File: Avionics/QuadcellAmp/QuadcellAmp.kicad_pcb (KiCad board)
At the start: 2 copper layers, 10 parts, among them U2 OPA1679

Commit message: quadcell 1014
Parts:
- removed U1: ~, Library:Quadcell
- added CR1: PDB-C142, PDB-C142:PDB-C142_ADP, F.Cu at (117.0, 74.0)
- added CR2: PDB-C142, PDB-C142:PDB-C142_ADP, F.Cu at (111.5, 80.3)
- added CR3: PDB-C142, PDB-C142:PDB-C142_ADP, F.Cu at (122.5, 80.0)
- added CR4: PDB-C142, PDB-C142:PDB-C142_ADP, F.Cu at (117.0, 86.0)
- added D1: 1N4001, Diode_THT:D_DO-41_SOD81_P10.16mm_Horizontal, F.Cu at (146.5, 59.5)
- added D2: 1N4001, Diode_THT:D_DO-41_SOD81_P10.16mm_Horizontal, F.Cu at (153.0, 71.0)
- added D3: 1N4001, Diode_THT:D_DO-41_SOD81_P10.16mm_Horizontal, F.Cu at (146.4, 63.5)
- added D4: 1N4001, Diode_THT:D_DO-41_SOD81_P10.16mm_Horizontal, F.Cu at (153.0, 82.0)
- added D5: 1N4001, Diode_THT:D_DO-41_SOD81_P10.16mm_Horizontal, F.Cu at (153.0, 75.0)
- added D6: 1N4001, Diode_THT:D_DO-41_SOD81_P10.16mm_Horizontal, F.Cu at (153.0, 86.0)
- added D7: 1N4001, Diode_THT:D_DO-41_SOD81_P10.16mm_Horizontal, F.Cu at (153.0, 92.2)
- added D8: 1N4001, Diode_THT:D_DO-41_SOD81_P10.16mm_Horizontal, F.Cu at (153.0, 96.5)
- added J1: Screw_Terminal_01x02, TerminalBlock:TerminalBlock_Xinya_XY308-2.54-2P_1x02_P2.54mm_Horizontal, F.Cu at (104.5, 67.0)
- added R10: 40 Ω, Resistor_THT:R_Axial_DIN0204_L3.6mm_D1.6mm_P1.90mm_Vertical, F.Cu at (169.8, 87.1)
- added R11: 1 kΩ, Resistor_THT:R_Axial_DIN0204_L3.6mm_D1.6mm_P1.90mm_Vertical, F.Cu at (147.6, 69.5)
- added R12: 40 Ω, Resistor_THT:R_Axial_DIN0204_L3.6mm_D1.6mm_P1.90mm_Vertical, F.Cu at (169.8, 93.4)
- added R13: 4.6k, Resistor_THT:R_Axial_DIN0204_L3.6mm_D1.6mm_P1.90mm_Vertical, F.Cu at (103.6, 77.3)
- added R14: 4.7k, Resistor_THT:R_Axial_DIN0204_L3.6mm_D1.6mm_P1.90mm_Vertical, F.Cu at (103.6, 80.5)
- added R5: 1 kΩ, Resistor_THT:R_Axial_DIN0204_L3.6mm_D1.6mm_P1.90mm_Vertical, F.Cu at (140.1, 64.5)
- added R6: 1 kΩ, Resistor_THT:R_Axial_DIN0204_L3.6mm_D1.6mm_P1.90mm_Vertical, F.Cu at (139.1, 98.5)
- added R7: 40 Ω, Resistor_THT:R_Axial_DIN0204_L3.6mm_D1.6mm_P1.90mm_Vertical, F.Cu at (162.6, 61.5)
- added R8: 1 kΩ, Resistor_THT:R_Axial_DIN0204_L3.6mm_D1.6mm_P1.90mm_Vertical, F.Cu at (145.1, 97.0)
- added R9: 40 Ω, Resistor_THT:R_Axial_DIN0204_L3.6mm_D1.6mm_P1.90mm_Vertical, F.Cu at (167.1, 73.0)
- R1, R2, R3, R4: value R -> 100 kΩ
- U2: value OPA1679 -> LM324N; footprint Package_DIP:DIP-14_W7.62mm -> LM324:N14
- moved C2 27.4 mm to (108.2, 97.5)
- moved R2 25.1 mm to (108.6, 89.0)
- moved U2 18.1 mm to (146.6, 88.7)
- moved C3 10.0 mm to (128.0, 99.5)
- moved C4 8.98 mm to (118.2, 99.0)
- moved R4 8.64 mm to (118.6, 94.0)
- moved R3 7.65 mm to (128.6, 91.5)
- moved C1 1.12 mm to (126.5, 67.0)
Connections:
- U2 pad 11: /V_NEG -> GND
- U2 pad 13: GND -> QUAD_GND
- U2 pad 2: GND -> QUAD_GND
- U2 pad 4: /V_POS -> +BATT
- U2 pad 6: GND -> QUAD_GND
- U2 pad 9: GND -> QUAD_GND
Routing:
- net GND: track 98.3 -> 0.00 mm
- net /Anode_D: track 88.0 -> 0.14 mm
- net /Anode_C: track 68.5 -> 0.14 mm
- net Net-(C4-Pad2): track 62.1 -> 0.00 mm
- net /Anode_A: track 58.8 -> 0.22 mm
- net /Anode_B: track 53.7 -> 0.00 mm
- net Net-(C3-Pad2): track 38.5 -> 0.00 mm
- net Net-(C2-Pad2): track 35.0 -> 0.00 mm
- net Net-(C1-Pad2): track 33.5 -> 0.00 mm
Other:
- board text added: "Quadcell Amp v2.0"
- board text removed: "Quadcell Amp v1.0"

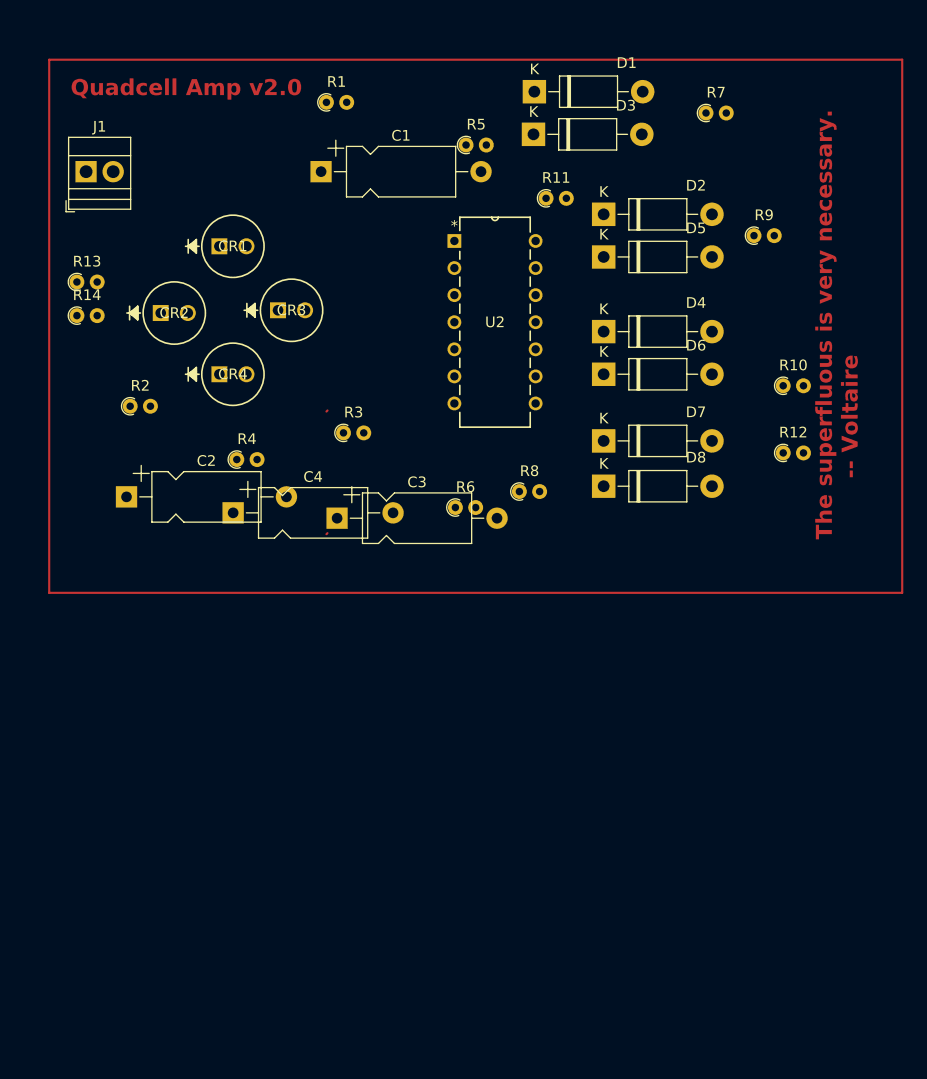
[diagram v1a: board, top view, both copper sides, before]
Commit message: Quadcell PD 2.0 finished
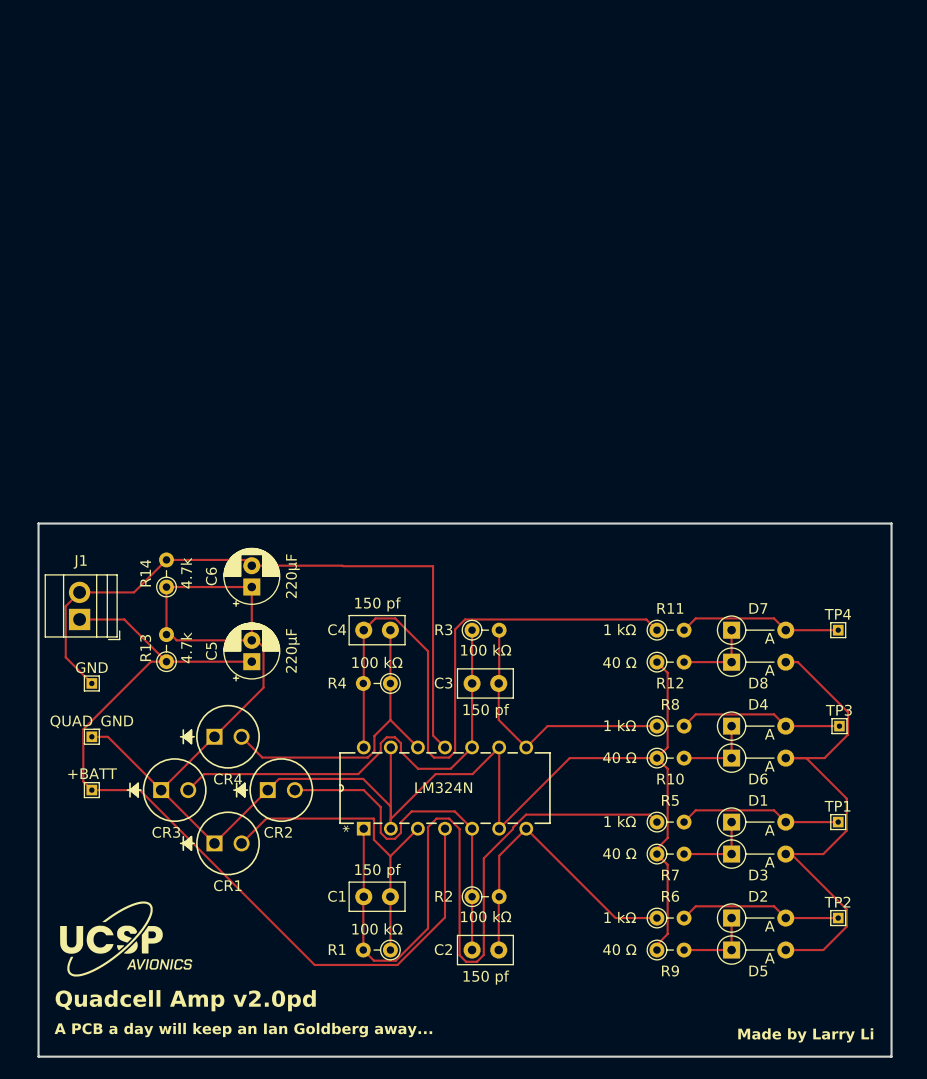
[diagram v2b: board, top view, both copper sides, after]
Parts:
- added +BATT: TestPoint, TestPoint:TestPoint_THTPad_1.0x1.0mm_Drill0.5mm, F.Cu at (105.0, 125.0)
- added C5: 220µF, Capacitor_THT:CP_Radial_D5.0mm_P2.00mm, F.Cu at (120.0, 113.0)
- added C6: 220µF, Capacitor_THT:CP_Radial_D5.0mm_P2.00mm, F.Cu at (120.0, 106.0)
- added G***: LOGO, UCSP:UCSP_avionics_logo, F.Cu at (107.0, 139.0)
- added GND: TestPoint, TestPoint:TestPoint_THTPad_1.0x1.0mm_Drill0.5mm, F.Cu at (105.0, 115.0)
- added QUAD_GND: TestPoint, TestPoint:TestPoint_THTPad_1.0x1.0mm_Drill0.5mm, F.Cu at (105.0, 120.0)
- added TP1: TestPoint, TestPoint:TestPoint_THTPad_1.0x1.0mm_Drill0.5mm, F.Cu at (175.0, 128.0)
- added TP2: TestPoint, TestPoint:TestPoint_THTPad_1.0x1.0mm_Drill0.5mm, F.Cu at (175.0, 137.0)
- added TP3: TestPoint, TestPoint:TestPoint_THTPad_1.0x1.0mm_Drill0.5mm, F.Cu at (175.1, 119.0)
- added TP4: TestPoint, TestPoint:TestPoint_THTPad_1.0x1.0mm_Drill0.5mm, F.Cu at (175.0, 110.0)
- C1, C2, C3, C4: value C -> 150 pf; footprint Capacitor_THT:CP_Axial_L10.0mm_D4.5mm_P15.00mm_Horizontal -> Capacitor_THT:C_Disc_D5.0mm_W2.5mm_P2.50mm
- D1, D2, D3, D4, D5, D6, D7, D8: value 1N4001 -> ~; footprint Diode_THT:D_DO-41_SOD81_P10.16mm_Horizontal -> Diode_THT:D_DO-35_SOD27_P5.08mm_Vertical_AnodeUp
- R1, R10, R11, R12, R14, R2, R3, R4, R5, R6, R7, R8, R9: footprint Resistor_THT:R_Axial_DIN0204_L3.6mm_D1.6mm_P1.90mm_Vertical -> Resistor_THT:R_Axial_DIN0204_L3.6mm_D1.6mm_P2.54mm_Vertical
- R13: value 4.6k -> 4.7k; footprint Resistor_THT:R_Axial_DIN0204_L3.6mm_D1.6mm_P1.90mm_Vertical -> Resistor_THT:R_Axial_DIN0204_L3.6mm_D1.6mm_P2.54mm_Vertical
- moved R1 79.7 mm to (133.0, 140.0), turned to 180 degrees
- moved D1 71.0 mm to (165.0, 128.0)
- moved D3 70.0 mm to (165.0, 131.0)
- moved R7 69.7 mm to (158.0, 131.0)
- moved C1 68.3 mm to (133.0, 135.0), turned to 180 degrees
- moved R9 67.6 mm to (158.0, 140.0)
- moved D2 67.1 mm to (165.0, 137.0)
- moved D5 66.1 mm to (165.0, 140.0)
- moved R5 66.0 mm to (158.0, 128.0)
- moved R2 56.1 mm to (140.7, 135.0)
- moved CR1 56.0 mm to (116.5, 130.0)
- moved C2 53.4 mm to (140.7, 140.0)
- moved CR3 46.3 mm to (111.5, 125.0)
- moved CR2 45.9 mm to (121.5, 125.0)
- moved R6 42.9 mm to (158.0, 137.0)
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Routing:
- net QUAD_GND: track 0.00 -> 158.4 mm
- net +BATT: track 0.00 -> 84.2 mm
- net Net-(C1-Pad2): track 0.00 -> 74.3 mm
- net Net-(C4-Pad2): track 0.00 -> 62.4 mm
- net GND: track 0.00 -> 61.7 mm
- net 3V3: track 0.00 -> 49.7 mm
- net /Anode_C: track 0.14 -> 42.6 mm
- net /Anode_B: track 0.00 -> 33.6 mm
- net /Anode_A: track 0.22 -> 30.0 mm
- net /Anode_D: track 0.14 -> 29.1 mm
- net Net-(C2-Pad2): track 0.00 -> 28.2 mm
- net Net-(C3-Pad2): track 0.00 -> 25.2 mm
- net Net-(D4-A): track 0.00 -> 15.5 mm
- net Net-(D7-A): track 0.00 -> 15.4 mm
- net Net-(D2-A): track 0.00 -> 15.4 mm
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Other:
- board outline added: 80 x 50 mm
- board text added: "A PCB a day will keep an Ian Goldberg away..."
- board text added: "Made by Larry Li"
- board text added: "Quadcell Amp v2.0pd"
- board text removed: "Quadcell Amp v2.0"
- board text removed: "The superfluous is very necessary. -- Voltaire"

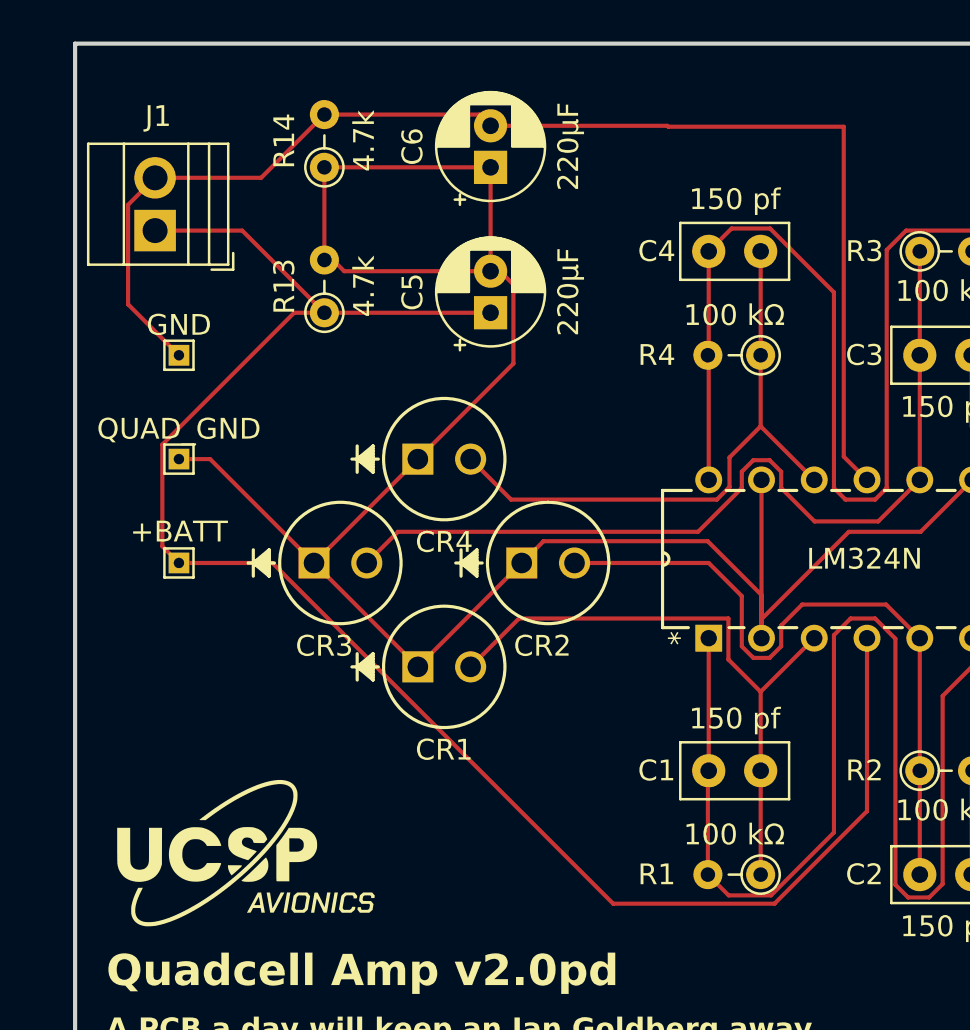
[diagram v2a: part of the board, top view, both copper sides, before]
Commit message: added USA flags to pulse footprint library
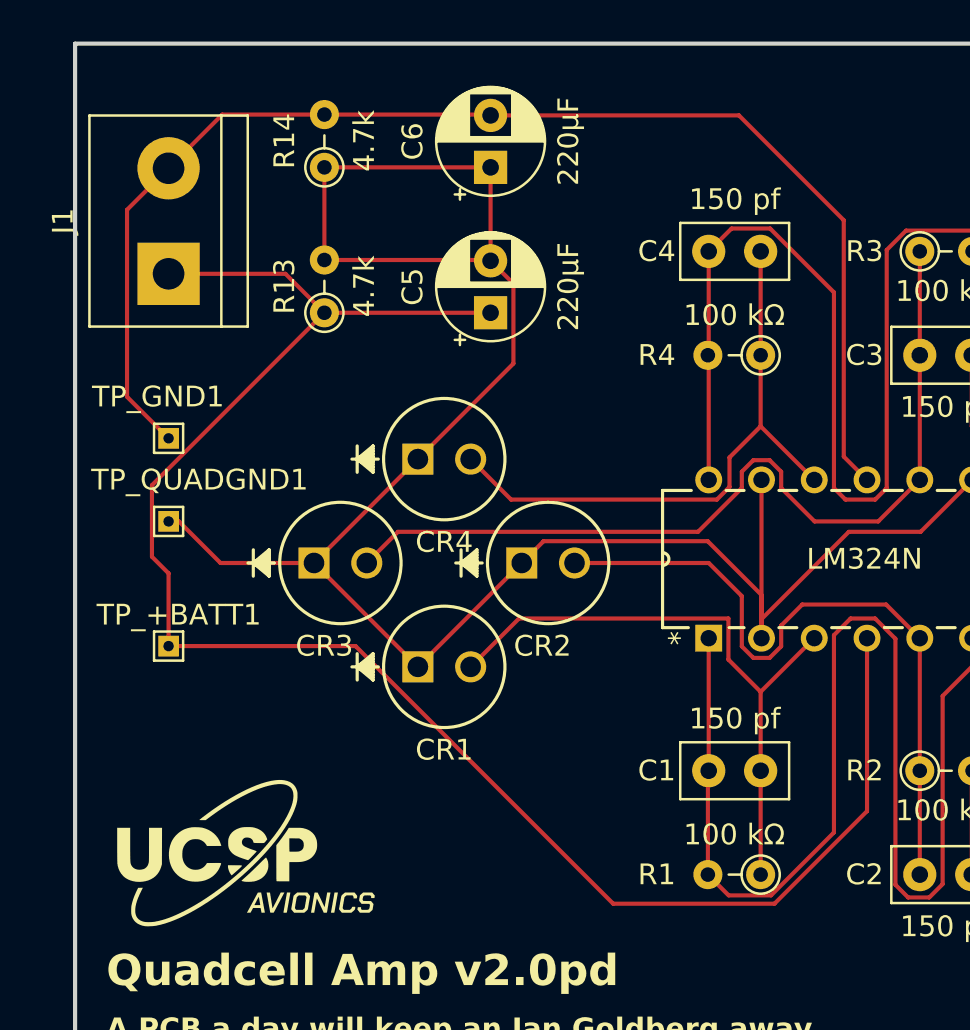
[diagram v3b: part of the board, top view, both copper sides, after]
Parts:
- removed +BATT, GND, QUAD_GND: TestPoint, TestPoint:TestPoint_THTPad_1.0x1.0mm_Drill0.5mm
- added TP_+BATT1: TestPoint, TestPoint:TestPoint_THTPad_1.0x1.0mm_Drill0.5mm, F.Cu at (104.5, 129.0)
- added TP_GND1: TestPoint, TestPoint:TestPoint_THTPad_1.0x1.0mm_Drill0.5mm, F.Cu at (104.5, 119.0)
- added TP_QUADGND1: TestPoint, TestPoint:TestPoint_THTPad_1.0x1.0mm_Drill0.5mm, F.Cu at (104.5, 123.0)
- C5, C6: footprint Capacitor_THT:CP_Radial_D5.0mm_P2.00mm -> Capacitor_THT:CP_Radial_D5.0mm_P2.50mm
- J1: footprint TerminalBlock:TerminalBlock_Xinya_XY308-2.54-2P_1x02_P2.54mm_Horizontal -> TerminalBlock:TerminalBlock_bornier-2_P5.08mm
- moved J1 2.18 mm to (104.5, 111.1)
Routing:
- net GND: track 61.7 -> 64.1 mm
- net +BATT: track 84.2 -> 85.0 mm
- net QUAD_GND: track 158.4 -> 157.6 mm

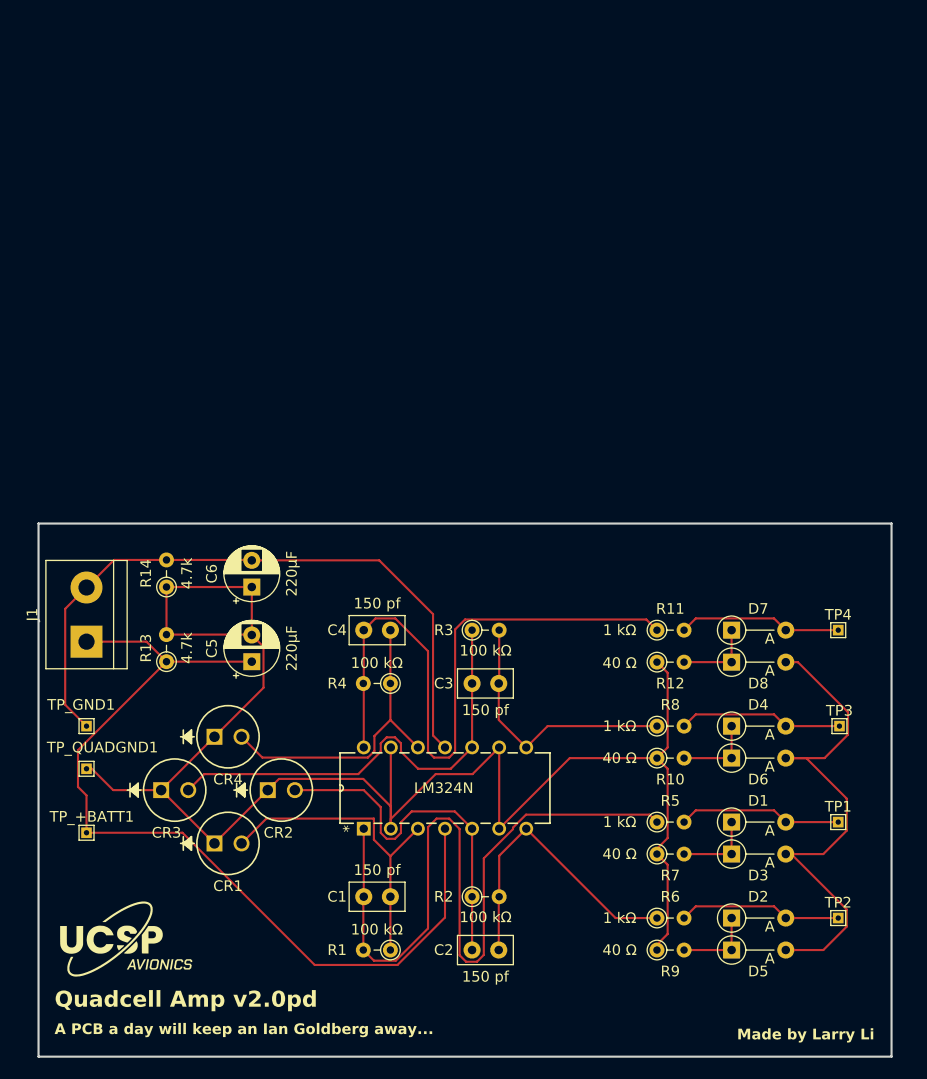
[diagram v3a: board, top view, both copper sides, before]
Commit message: flipped op amp signs :/
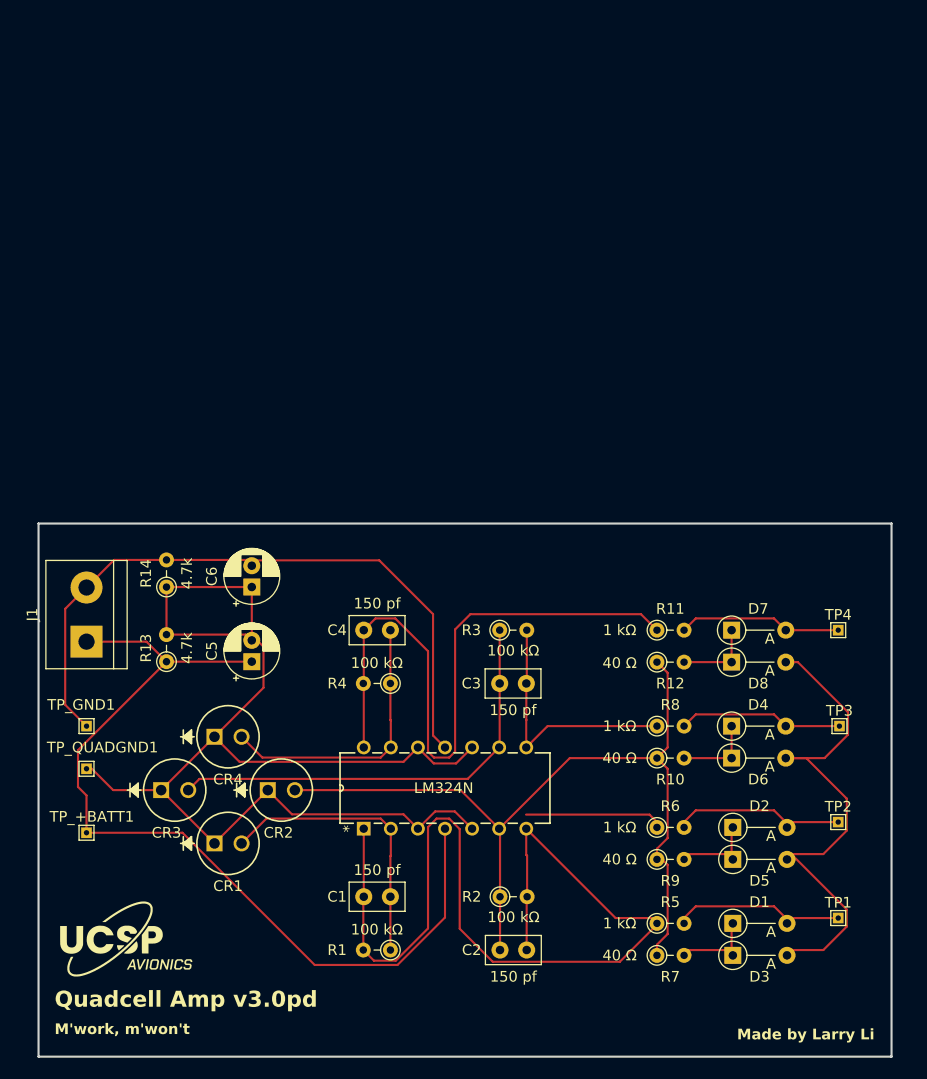
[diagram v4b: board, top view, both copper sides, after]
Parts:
- C5, C6: footprint Capacitor_THT:CP_Radial_D5.0mm_P2.50mm -> Capacitor_THT:CP_Radial_D5.0mm_P2.00mm
- moved D1 9.50 mm to (165.1, 137.5)
- moved D3 9.50 mm to (165.1, 140.5)
- moved R5 9.50 mm to (158.0, 137.5)
- moved R7 9.50 mm to (158.0, 140.5)
- moved TP1 9.00 mm to (175.0, 137.0)
- moved TP2 9.00 mm to (175.0, 128.0)
- moved D2 8.50 mm to (165.1, 128.5)
- moved D5 8.50 mm to (165.1, 131.5)
- moved R6 8.50 mm to (158.0, 128.5)
- moved R9 8.50 mm to (158.0, 131.5)
- moved C2 2.62 mm to (143.3, 140.0)
- moved R2 2.62 mm to (143.3, 135.0)
- moved C3 2.59 mm to (143.2, 115.0)
- moved R3 2.59 mm to (143.2, 110.0)
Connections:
- U2 pad 10: /Anode_C -> QUAD_GND
- U2 pad 12: /Anode_D -> QUAD_GND
- U2 pad 13: QUAD_GND -> /Anode_D
- U2 pad 2: QUAD_GND -> /Anode_A
- U2 pad 3: /Anode_A -> QUAD_GND
- U2 pad 5: /Anode_B -> QUAD_GND
- U2 pad 6: QUAD_GND -> /Anode_B
- U2 pad 9: QUAD_GND -> /Anode_C
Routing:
- net Net-(C2-Pad2): track 28.2 -> 39.7 mm
- net Net-(C1-Pad2): track 74.3 -> 63.1 mm
- net QUAD_GND: track 157.6 -> 161.5 mm
- net /Anode_A: track 30.0 -> 26.8 mm
- net /Anode_D: track 29.1 -> 26.2 mm
- net /Anode_B: track 33.6 -> 31.6 mm
- net Net-(C3-Pad2): track 25.2 -> 24.1 mm
- net /Anode_C: track 42.6 -> 41.9 mm
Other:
- board text added: "M'work, m'won't"
- board text added: "Quadcell Amp v3.0pd"
- board text removed: "A PCB a day will keep an Ian Goldberg away..."
- board text removed: "Quadcell Amp v2.0pd"
